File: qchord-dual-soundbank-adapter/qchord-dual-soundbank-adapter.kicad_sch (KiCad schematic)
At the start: 4 parts, among them SW1 SW_DIP_x01, U1 MX23C8100M, U2 M29F160FB5AN6F2

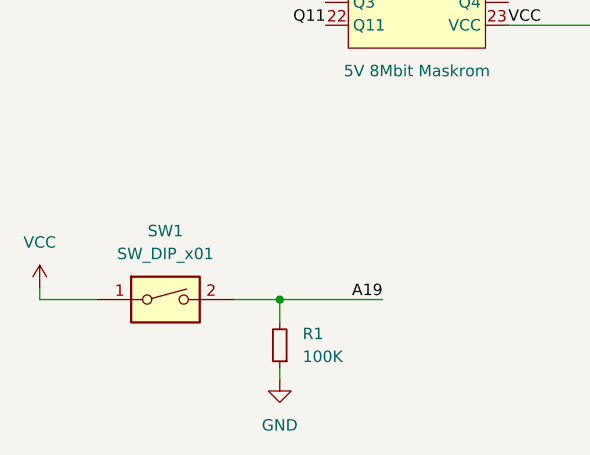
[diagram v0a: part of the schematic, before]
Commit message: pullup instead of pulldown by default
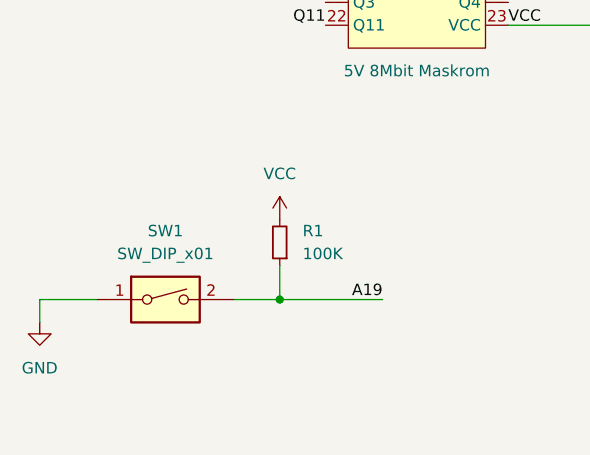
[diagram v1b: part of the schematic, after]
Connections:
- net A19: now also R1.1; no longer R1.2
- net GND: now also SW1.1; no longer R1.1
- net VCC: now also R1.2; no longer SW1.1
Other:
- moved on the sheet: R1
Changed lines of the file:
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@@
     (stroke (width 0) (type default))
   )
-  (wire (pts (xy 57.15 119.38) (xy 57.15 120.65))
+  (wire (pts (xy 57.15 107.95) (xy 57.15 111.76))
     (stroke (width 0) (type default))
   )
@@
     (stroke (width 0) (type default))
   )
-  (wire (pts (xy 57.15 114.3) (xy 57.15 111.76))
-    (stroke (width 0) (type default))
-  )
-  (wire (pts (xy 30.48 110.49) (xy 30.48 111.76))
+  (wire (pts (xy 30.48 111.76) (xy 30.48 114.3))
     (stroke (width 0) (type default))
   )
@@
     (effects (font (size 1.27 1.27)) (justify left bottom))
   )
-  (symbol (lib_id "power:GND") (at 57.15 120.65 0) (unit 1)
+  (symbol (lib_id "power:GND") (at 30.48 114.3 0) (unit 1)
     (in_bom yes) (on_board yes) (dnp no) (fields_autoplaced)
-    (property "Reference" "#PWR04" (at 57.15 127 0)
-      (effects (font (size 1.27 1.27)) hide)
-    )
-    (property "Value" "GND" (at 57.15 125.73 0)
-      (effects (font (size 1.27 1.27)))
-    )
-    (property "Footprint" "" (at 57.15 120.65 0)
-      (effects (font (size 1.27 1.27)) hide)
-    )
-    (property "Datasheet" "" (at 57.15 120.65 0)
-      (effects (font (size 1.27 1.27)) hide)
-    )
-    (pin "1")
-    (instances
-      (project "soundbank"
+    (property "Reference" "#PWR04" (at 30.48 120.65 0)
+      (effects (font (size 1.27 1.27)) hide)
+    )
+    (property "Value" "GND" (at 30.48 119.38 0)
+      (effects (font (size 1.27 1.27)))
+    )
+    (property "Footprint" "" (at 30.48 114.3 0)
+      (effects (font (size 1.27 1.27)) hide)
+    )
+    (property "Datasheet" "" (at 30.48 114.3 0)
+      (effects (font (size 1.27 1.27)) hide)
+    )
+    (pin "1")
+    (instances
+      (project "qchord-dual-soundbank-adapter"
         (path "/8abe2c0e-d2a7-4d2b-9391-554ca5a506a1"
           (reference "#PWR04") (unit 1)
@@
     (pin "2")
     (instances
-      (project "soundbank"
+      (project "qchord-dual-soundbank-adapter"
         (path "/8abe2c0e-d2a7-4d2b-9391-554ca5a506a1"
           (reference "SW1") (unit 1)
@@
     )
   )
-  (symbol (lib_id "power:VCC") (at 30.48 110.49 0) (unit 1)
+  (symbol (lib_id "power:VCC") (at 57.15 102.87 0) (unit 1)
     (in_bom yes) (on_board yes) (dnp no) (fields_autoplaced)
-    (property "Reference" "#PWR03" (at 30.48 114.3 0)
-      (effects (font (size 1.27 1.27)) hide)
-    )
-    (property "Value" "VCC" (at 30.48 105.41 0)
-      (effects (font (size 1.27 1.27)))
-    )
-    (property "Footprint" "" (at 30.48 110.49 0)
-      (effects (font (size 1.27 1.27)) hide)
-    )
-    (property "Datasheet" "" (at 30.48 110.49 0)
-      (effects (font (size 1.27 1.27)) hide)
-    )
-    (pin "1")
-    (instances
-      (project "soundbank"
+    (property "Reference" "#PWR03" (at 57.15 106.68 0)
+      (effects (font (size 1.27 1.27)) hide)
+    )
+    (property "Value" "VCC" (at 57.15 97.79 0)
+      (effects (font (size 1.27 1.27)))
+    )
+    (property "Footprint" "" (at 57.15 102.87 0)
+      (effects (font (size 1.27 1.27)) hide)
+    )
+    (property "Datasheet" "" (at 57.15 102.87 0)
+      (effects (font (size 1.27 1.27)) hide)
+    )
+    (pin "1")
+    (instances
+      (project "qchord-dual-soundbank-adapter"
         (path "/8abe2c0e-d2a7-4d2b-9391-554ca5a506a1"
           (reference "#PWR03") (unit 1)
@@
     (pin "1")
     (instances
-      (project "soundbank"
+      (project "qchord-dual-soundbank-adapter"
         (path "/8abe2c0e-d2a7-4d2b-9391-554ca5a506a1"
           (reference "#PWR01") (unit 1)
@@
     )
   )
-  (symbol (lib_id "Device:R_Small") (at 57.15 116.84 180) (unit 1)
+  (symbol (lib_id "Device:R_Small") (at 57.15 105.41 180) (unit 1)
     (in_bom yes) (on_board yes) (dnp no) (fields_autoplaced)
-    (property "Reference" "R1" (at 59.69 115.57 0)
+    (property "Reference" "R1" (at 59.69 104.14 0)
       (effects (font (size 1.27 1.27)) (justify right))
     )
-    (property "Value" "100K" (at 59.69 118.11 0)
+    (property "Value" "100K" (at 59.69 106.68 0)
       (effects (font (size 1.27 1.27)) (justify right))
     )
-    (property "Footprint" "Resistor_SMD:R_0805_2012Metric_Pad1.20x1.40mm_HandSolder" (at 57.15 116.84 0)
-      (effects (font (size 1.27 1.27)) hide)
-    )
-    (property "Datasheet" "~" (at 57.15 116.84 0)
+    (property "Footprint" "Resistor_SMD:R_0805_2012Metric_Pad1.20x1.40mm_HandSolder" (at 57.15 105.41 0)
+      (effects (font (size 1.27 1.27)) hide)
+    )
+    (property "Datasheet" "~" (at 57.15 105.41 0)
       (effects (font (size 1.27 1.27)) hide)
     )
@@
     (pin "2")
     (instances
-      (project "soundbank"
+      (project "qchord-dual-soundbank-adapter"
         (path "/8abe2c0e-d2a7-4d2b-9391-554ca5a506a1"
           (reference "R1") (unit 1)
@@
     (pin "1")
     (instances
-      (project "soundbank"
+      (project "qchord-dual-soundbank-adapter"
         (path "/8abe2c0e-d2a7-4d2b-9391-554ca5a506a1"
           (reference "#PWR02") (unit 1)
@@
     (pin "9")
     (instances
-      (project "soundbank"
+      (project "qchord-dual-soundbank-adapter"
         (path "/8abe2c0e-d2a7-4d2b-9391-554ca5a506a1"
           (reference "U1") (unit 1)
@@
     (pin "9")
     (instances
-      (project "soundbank"
+      (project "qchord-dual-soundbank-adapter"
         (path "/8abe2c0e-d2a7-4d2b-9391-554ca5a506a1"
           (reference "U2") (unit 1)
